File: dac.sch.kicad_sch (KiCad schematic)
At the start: 2 parts, among them IC1 ES9023P, U16 NUCLEO-F446RE

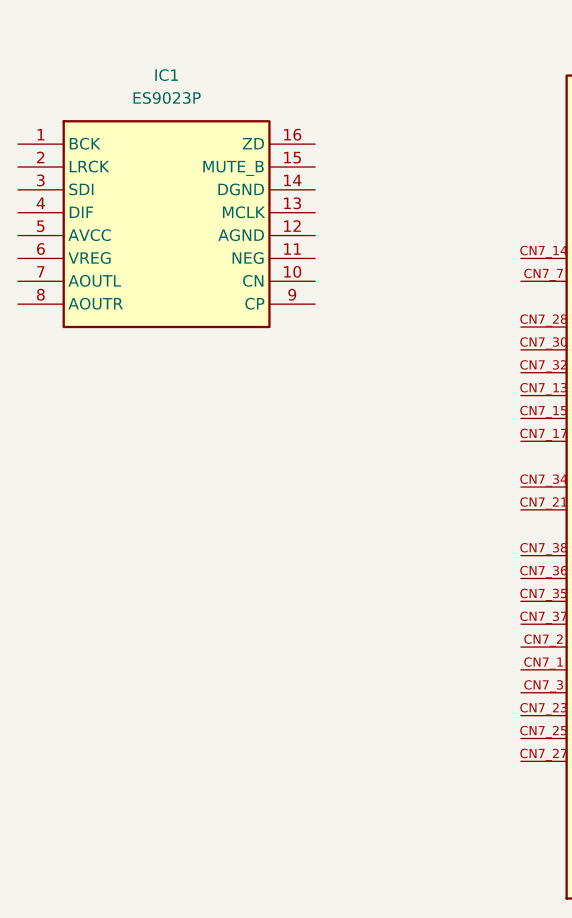
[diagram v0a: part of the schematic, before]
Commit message: modelpathssdefuined
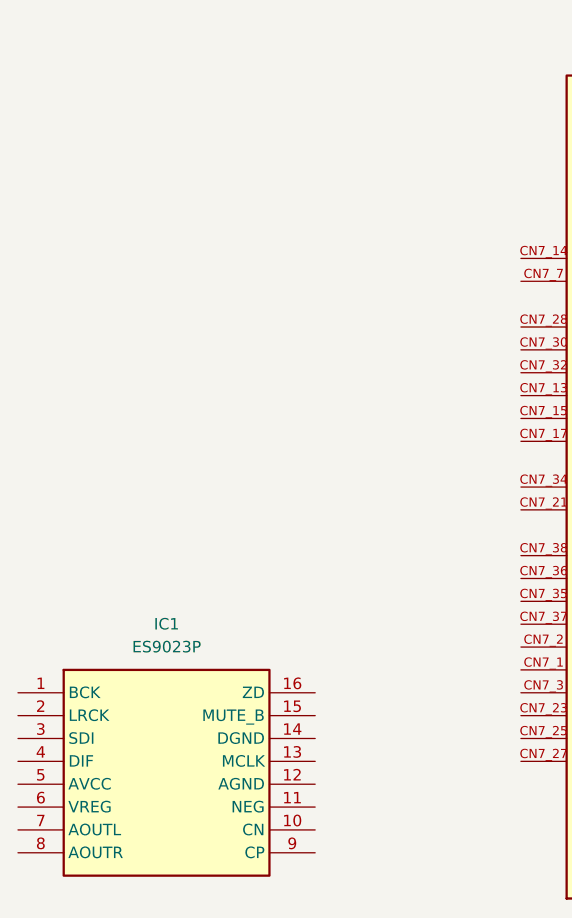
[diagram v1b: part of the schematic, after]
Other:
- moved on the sheet: IC1
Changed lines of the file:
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@@
 	(symbol
 		(lib_id "esp32lib:ES9023P")
-		(at 132.08 55.88 0)
+		(at 132.08 116.84 0)
 		(unit 1)
 		(exclude_from_sim no)
@@
 		(fields_autoplaced yes)
 		(property "Reference" "IC1"
-			(at 148.59 48.26 0)
+			(at 148.59 109.22 0)
 			(effects
 				(font
@@
 		)
 		(property "Value" "ES9023P"
-			(at 148.59 50.8 0)
+			(at 148.59 111.76 0)
 			(effects
 				(font
@@
 		)
 		(property "Footprint" "customfootprints:SOIC127P600X175-16N"
-			(at 161.29 150.8 0)
+			(at 161.29 211.76 0)
 			(effects
 				(font
@@
 		)
 		(property "Datasheet" ""
-			(at 161.29 250.8 0)
+			(at 161.29 311.76 0)
 			(effects
 				(font
@@
 		)
 		(property "Description" "Audio D/A Converter ICs Sabre 2V RMS stereo DAC"
-			(at 132.08 55.88 0)
+			(at 132.08 116.84 0)
 			(effects
 				(font
@@
 		)
 		(property "Height" "1.75"
-			(at 161.29 450.8 0)
+			(at 161.29 511.76 0)
 			(effects
 				(font
@@
 		)
 		(property "Mouser Part Number" "460-ES9023P"
-			(at 161.29 550.8 0)
+			(at 161.29 611.76 0)
 			(effects
 				(font
@@
 		)
 		(property "Mouser Price/Stock" "https://www.mouser.co.uk/ProductDetail/ESS-Technology/ES9023P?qs=sPbYRqrBIVn%252BcPkDS1h3%252BQ%3D%3D"
-			(at 161.29 650.8 0)
+			(at 161.29 711.76 0)
 			(effects
 				(font
@@
 		)
 		(property "Manufacturer_Name" "ESS Technology"
-			(at 161.29 750.8 0)
+			(at 161.29 811.76 0)
 			(effects
 				(font
@@
 		)
 		(property "Manufacturer_Part_Number" "ES9023P"
-			(at 161.29 850.8 0)
+			(at 161.29 911.76 0)
 			(effects
 				(font

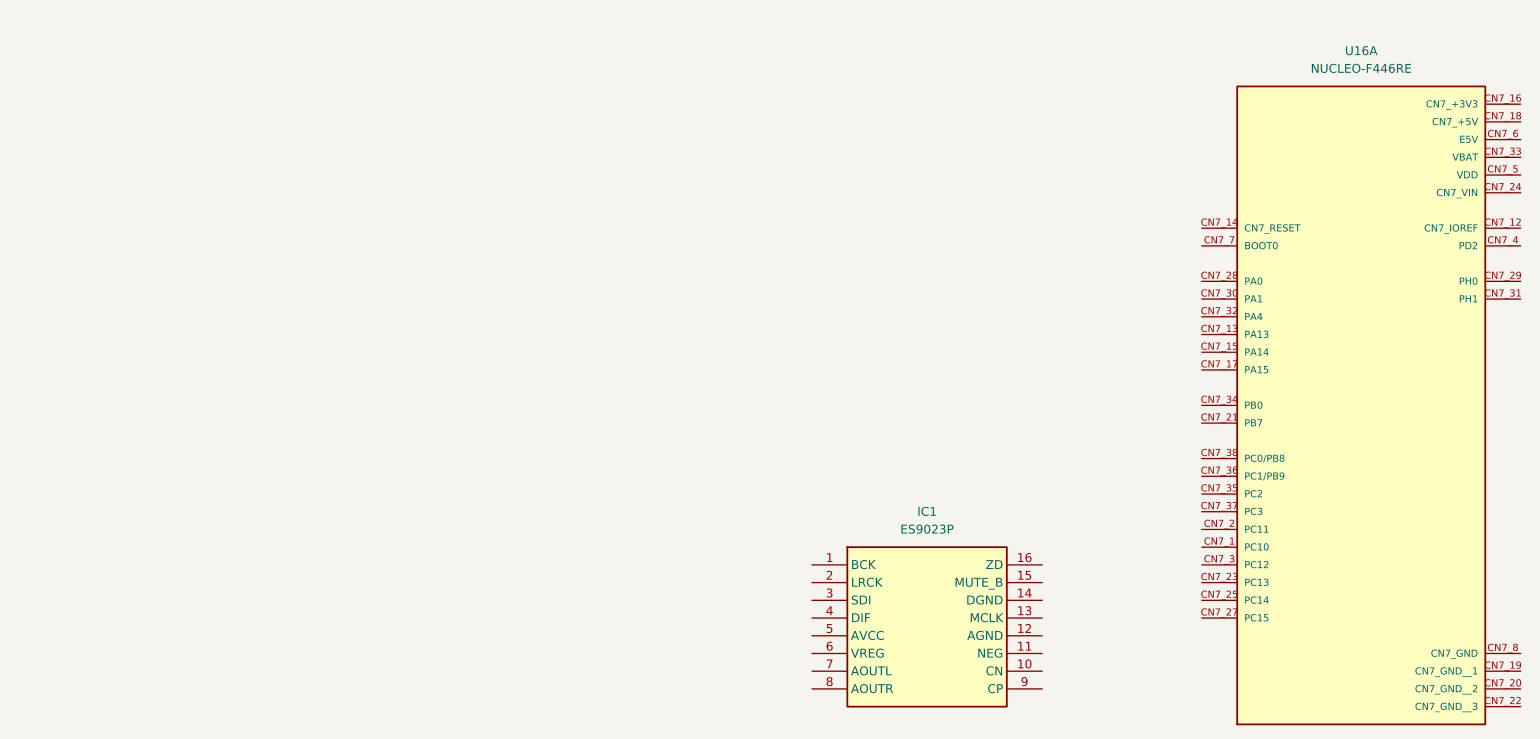
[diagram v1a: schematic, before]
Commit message: updated DacSheet
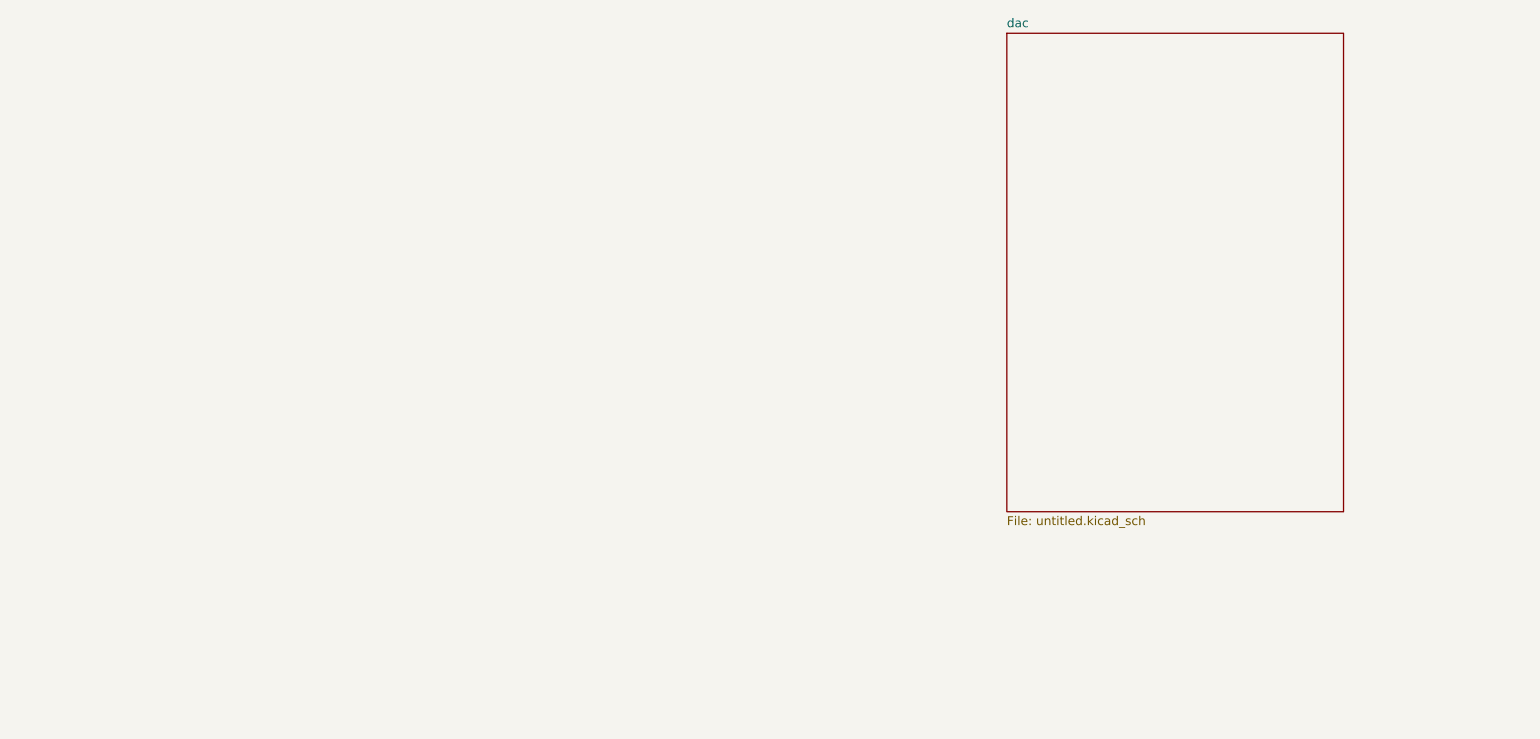
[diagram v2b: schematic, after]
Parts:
- removed IC1: ES9023P, customfootprints:SOIC127P600X175-16N, symbol esp32lib:ES9023P
- removed U16: NUCLEO-F446RE, customfootprints:MODULE_NUCLEO-F446RE, symbol esp32lib:NUCLEO-F446RE
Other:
- added sheet dac (untitled.kicad_sch)

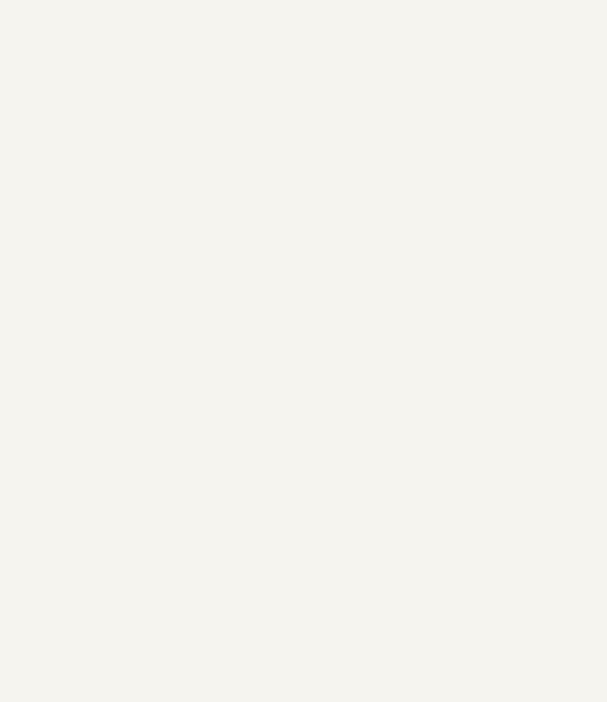
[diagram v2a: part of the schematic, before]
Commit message: added codec
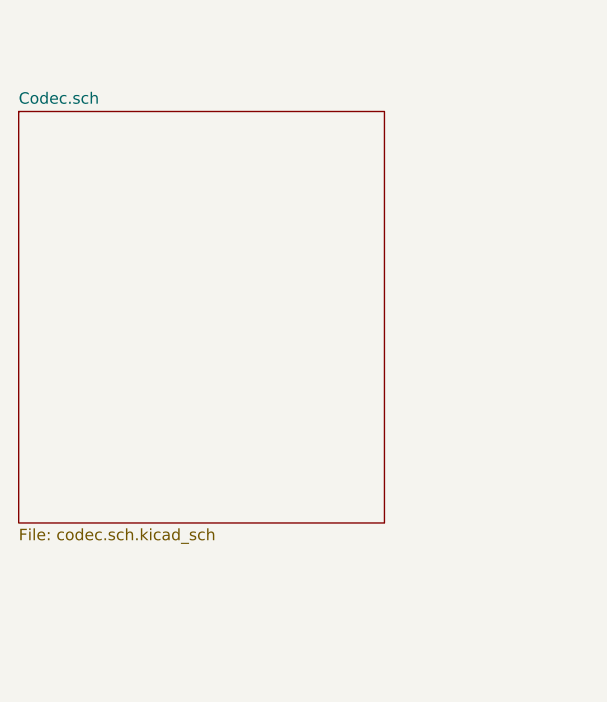
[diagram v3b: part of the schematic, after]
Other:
- added sheet Codec.sch (codec.sch.kicad_sch)
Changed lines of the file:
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@@
+		)
+	)
+	(sheet
+		(at 17.78 48.26)
+		(size 40.64 45.72)
+		(fields_autoplaced yes)
+		(stroke
+			(width 0.1524)
+			(type solid)
+		)
+		(fill
+			(color 0 0 0 0.0000)
+		)
+		(property "Sheetname" "Codec.sch"
+			(at 17.78 47.5484 0)
+			(effects
+				(font
+					(size 1.27 1.27)
+				)
+				(justify left bottom)
+			)
+		)
+		(property "Sheetfile" "codec.sch.kicad_sch"
+			(at 17.78 94.5646 0)
+			(effects
+				(font
+					(size 1.27 1.27)
+				)
+				(justify left top)
+			)
+		)
+		(instances
+			(project "esp32"
+				(path "/c4754426-a41b-4341-9d09-2e389619f3d6/a94728e7-5369-4898-bc9c-adaf2aafacfb"
+					(page "8")
+				)
+			)
 		)
 	)
